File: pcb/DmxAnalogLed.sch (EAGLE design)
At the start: 61 parts, among them IC2 7805TV, J1 RS485, J2 POWER_JACKPTH, J3 RS485, Q1 16MHz 10ppm, U1 ARDUINO_LEONARDO-REV3B_SMARTP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, U2 SN75176ASOIC, X1 USBPTH

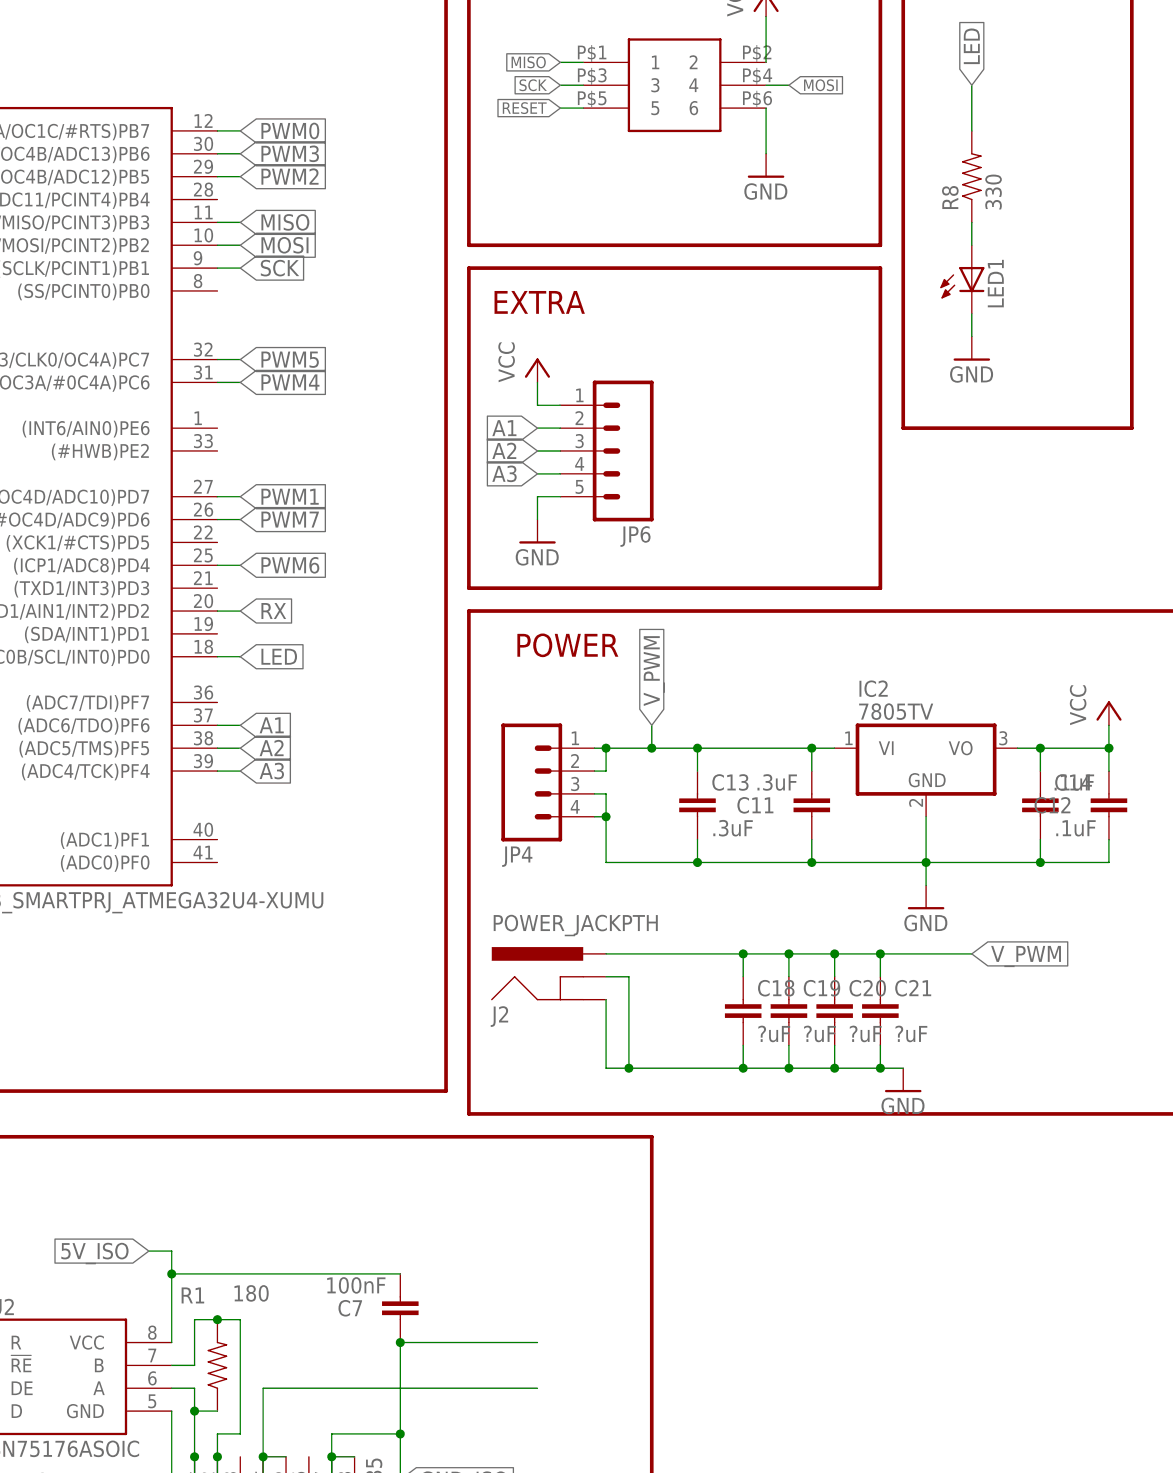
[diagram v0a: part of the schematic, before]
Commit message: Update component values on PCB
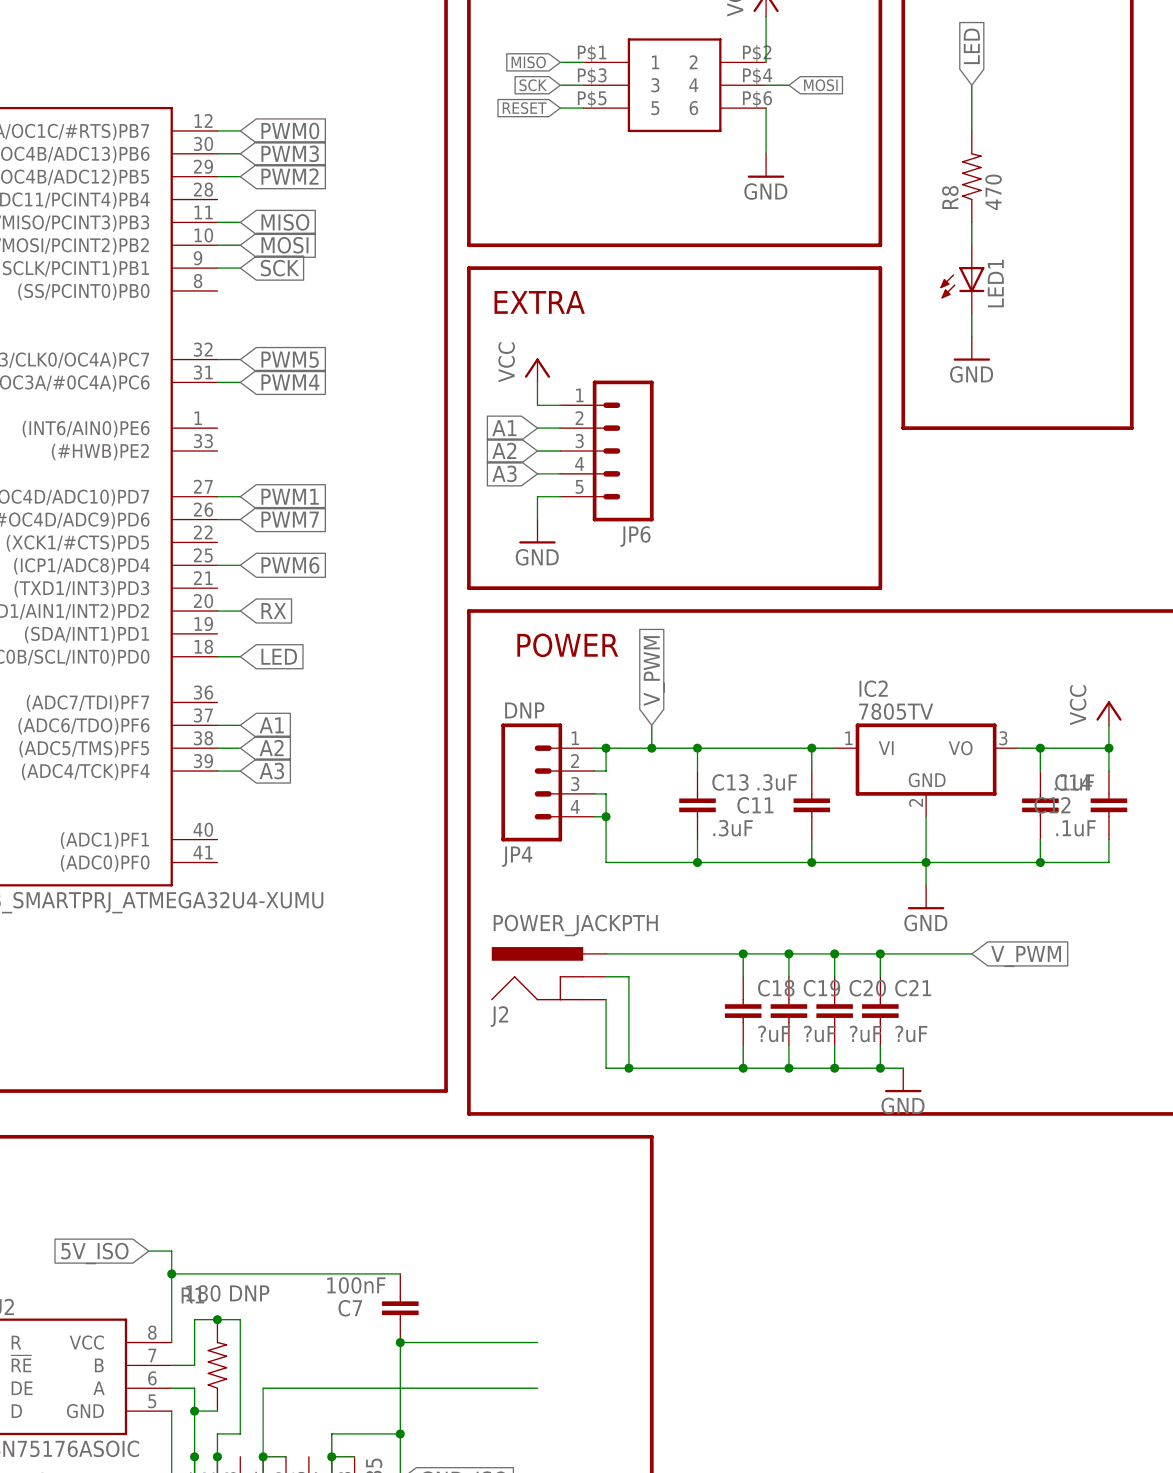
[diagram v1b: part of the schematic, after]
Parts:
- JP4: value (none) -> DNP
- R1: value 180 -> 180 DNP
- R8: value 330 -> 470
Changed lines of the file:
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@@
 <parts>
 <part name="U2" library="reprap" deviceset="SN75176A" device="SOIC"/>
-<part name="R1" library="SparkFun" deviceset="RESISTOR" device="" value="180"/>
+<part name="R1" library="SparkFun" deviceset="RESISTOR" device="" value="180 DNP"/>
 <part name="R2" library="SparkFun" deviceset="RESISTOR" device="" value="10k"/>
-<part name="R8" library="SparkFun" deviceset="RESISTOR" device="" value="330"/>
+<part name="R8" library="SparkFun" deviceset="RESISTOR" device="" value="470"/>
 <part name="GND12" library="supply1" deviceset="GND" device=""/>
 <part name="C7" library="SparkFun" deviceset="CAP" device="0805" value="100nF"/>
@@
 <part name="JP2" library="SparkFun" deviceset="M08" device="3.5MM-8"/>
 <part name="JP3" library="SparkFun" deviceset="M08" device="3.5MM-8"/>
-<part name="JP4" library="SparkFun" deviceset="M04" device="SCREW"/>
+<part name="JP4" library="SparkFun" deviceset="M04" device="SCREW" value="DNP"/>
 <part name="U$10" library="blinkiverse" deviceset="DC_DC_ISOLATED_0505" device=""/>
 <part name="P+8" library="supply1" deviceset="VCC" device=""/>

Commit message: Get RevB ready
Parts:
- removed C18, C19, C20, C21: ?uF, SparkFun:CAP1210
- removed JP4: DNP, SparkFun:M04SCREW
- added C22: .1uF, SparkFun:CAP0805
- added C23, C24, C25, C26: (no value), SparkFun:CAP_POLE
- C3: value 10uF -> .1uF
- C5, C6: value 100nF -> .1uF
- IC2: value 7805TV -> 7805DT; device linear:7805TV -> linear:7805DT
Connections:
- removed net V_PWM: C11.2, C13.1, C18.1, C19.1, C20.1, C21.1, IC2.VI, J2.PWR, JP2.1, JP2.3, JP2.5, JP2.7, JP3.1, JP3.3, JP3.5, JP3.7, JP4.1, JP4.2
- new net V_IN: C11.2, C13.1, C23.+, C24.+, C25.+, C26.+, IC2.VI, J2.PWR, JP2.1, JP2.3, JP2.5, JP2.7, JP3.1, JP3.3, JP3.5, JP3.7
- net GND: now also C22.1, C23.-, C24.-, C25.-, C26.-; no longer C18.2, C19.2, C20.2, C21.2, JP4.3, JP4.4
- net VCC: now also C22.2

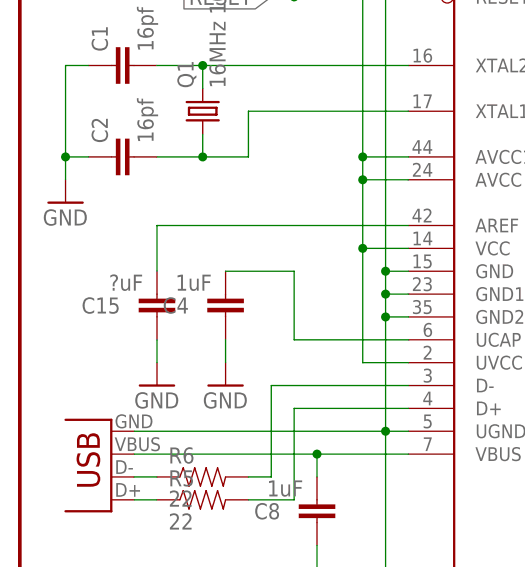
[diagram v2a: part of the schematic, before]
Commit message: RevB candidate; fixes ground plane, isolation, regulator placement, silk.
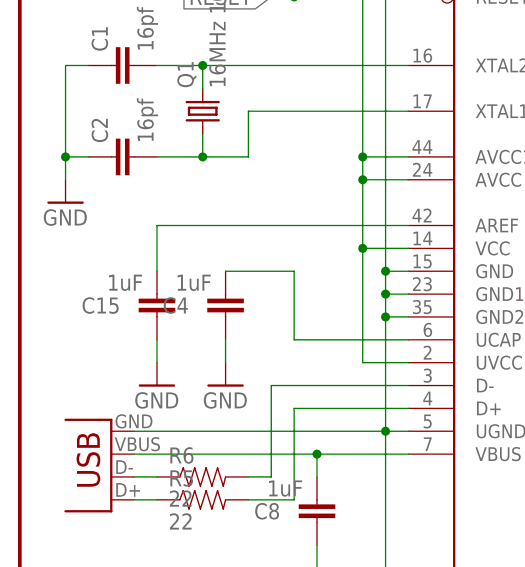
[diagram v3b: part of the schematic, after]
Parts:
- C15: value ?uF -> 1uF
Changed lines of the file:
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@@
 <part name="C13" library="SparkFun" deviceset="CAP" device="1210" value=".3uF"/>
 <part name="C14" library="SparkFun" deviceset="CAP" device="1210" value=".1uF"/>
-<part name="C15" library="SparkFun" deviceset="CAP" device="0805" value="?uF"/>
+<part name="C15" library="SparkFun" deviceset="CAP" device="0805" value="1uF"/>
 <part name="GND3" library="supply1" deviceset="GND" device=""/>
 <part name="C16" library="SparkFun" deviceset="CAP" device="1210" value="4.7uF"/>

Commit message: Make the software faster.
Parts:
- C12, C14, C22, C3, C5, C6: value .1uF -> 100nF
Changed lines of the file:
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@@
 <part name="R5" library="SparkFun" deviceset="RESISTOR" device="" value="22"/>
 <part name="R6" library="SparkFun" deviceset="RESISTOR" device="" value="22"/>
-<part name="C3" library="SparkFun" deviceset="CAP" device="0805" value=".1uF"/>
-<part name="C5" library="SparkFun" deviceset="CAP" device="0805" value=".1uF"/>
-<part name="C6" library="SparkFun" deviceset="CAP" device="0805" value=".1uF"/>
+<part name="C3" library="SparkFun" deviceset="CAP" device="0805" value="100nF"/>
+<part name="C5" library="SparkFun" deviceset="CAP" device="0805" value="100nF"/>
+<part name="C6" library="SparkFun" deviceset="CAP" device="0805" value="100nF"/>
 <part name="GND4" library="supply1" deviceset="GND" device=""/>
 <part name="P+2" library="supply1" deviceset="VCC" device=""/>
@@
 <part name="GND21" library="supply1" deviceset="GND" device=""/>
 <part name="C11" library="SparkFun" deviceset="CAP" device="0805" value=".3uF"/>
-<part name="C12" library="SparkFun" deviceset="CAP" device="0805" value=".1uF"/>
+<part name="C12" library="SparkFun" deviceset="CAP" device="0805" value="100nF"/>
 <part name="JP6" library="SparkFun" deviceset="M05" device="PTH"/>
 <part name="P+3" library="supply1" deviceset="VCC" device=""/>
@@
 <part name="P+4" library="supply1" deviceset="VCC" device=""/>
 <part name="C13" library="SparkFun" deviceset="CAP" device="1210" value=".3uF"/>
-<part name="C14" library="SparkFun" deviceset="CAP" device="1210" value=".1uF"/>
+<part name="C14" library="SparkFun" deviceset="CAP" device="1210" value="100nF"/>
 <part name="C15" library="SparkFun" deviceset="CAP" device="0805" value="1uF"/>
 <part name="GND3" library="supply1" deviceset="GND" device=""/>
@@
 <part name="R16" library="SparkFun" deviceset="RESISTOR" device="" value="10K"/>
 <part name="IC2" library="linear" deviceset="78*" device="DT" technology="05"/>
-<part name="C22" library="SparkFun" deviceset="CAP" device="0805" value=".1uF"/>
+<part name="C22" library="SparkFun" deviceset="CAP" device="0805" value="100nF"/>
 <part name="C23" library="SparkFun" deviceset="CAP_POL" device="E"/>
 <part name="C24" library="SparkFun" deviceset="CAP_POL" device="E"/>

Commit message: Change library name, too
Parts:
- U$1, U$3, U$4, U$5, U$6, U$7, U$8, U$9: device blinkiverse:N_MOSFET -> blinkinlabs:N_MOSFET
- U$10: device blinkiverse:DC_DC_ISOLATED_0505 -> blinkinlabs:DC_DC_ISOLATED_0505
- U1: device blinkiverse:ARDUINO_LEONARDO-REV3B_SMARTPRJ_ATMEGA32U4-XUMU -> blinkinlabs:ARDUINO_LEONARDO-REV3B_SMARTPRJ_ATMEGA32U4-XUMU
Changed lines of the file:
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@@
 <part name="P+5" library="supply1" deviceset="VCC" device=""/>
 <part name="GND10" library="supply1" deviceset="GND" device=""/>
-<part name="U1" library="blinkiverse" deviceset="ARDUINO_LEONARDO-REV3B_SMARTPRJ_ATMEGA32U4-XU" device="MU"/>
+<part name="U1" library="blinkinlabs" deviceset="ARDUINO_LEONARDO-REV3B_SMARTPRJ_ATMEGA32U4-XU" device="MU"/>
 <part name="P+1" library="supply1" deviceset="VCC" device=""/>
 <part name="GND1" library="supply1" deviceset="GND" device=""/>
@@
 <part name="GND6" library="supply1" deviceset="GND" device=""/>
 <part name="J3" library="con-amp" deviceset="520426-4" device="" value="RS485"/>
-<part name="U$1" library="blinkiverse" deviceset="N_MOSFET" device=""/>
+<part name="U$1" library="blinkinlabs" deviceset="N_MOSFET" device=""/>
 <part name="GND7" library="supply1" deviceset="GND" device=""/>
-<part name="U$3" library="blinkiverse" deviceset="N_MOSFET" device=""/>
+<part name="U$3" library="blinkinlabs" deviceset="N_MOSFET" device=""/>
 <part name="GND9" library="supply1" deviceset="GND" device=""/>
-<part name="U$4" library="blinkiverse" deviceset="N_MOSFET" device=""/>
+<part name="U$4" library="blinkinlabs" deviceset="N_MOSFET" device=""/>
 <part name="GND11" library="supply1" deviceset="GND" device=""/>
-<part name="U$5" library="blinkiverse" deviceset="N_MOSFET" device=""/>
+<part name="U$5" library="blinkinlabs" deviceset="N_MOSFET" device=""/>
 <part name="GND13" library="supply1" deviceset="GND" device=""/>
-<part name="U$6" library="blinkiverse" deviceset="N_MOSFET" device=""/>
+<part name="U$6" library="blinkinlabs" deviceset="N_MOSFET" device=""/>
 <part name="GND14" library="supply1" deviceset="GND" device=""/>
-<part name="U$7" library="blinkiverse" deviceset="N_MOSFET" device=""/>
+<part name="U$7" library="blinkinlabs" deviceset="N_MOSFET" device=""/>
 <part name="GND15" library="supply1" deviceset="GND" device=""/>
-<part name="U$8" library="blinkiverse" deviceset="N_MOSFET" device=""/>
+<part name="U$8" library="blinkinlabs" deviceset="N_MOSFET" device=""/>
 <part name="GND16" library="supply1" deviceset="GND" device=""/>
-<part name="U$9" library="blinkiverse" deviceset="N_MOSFET" device=""/>
+<part name="U$9" library="blinkinlabs" deviceset="N_MOSFET" device=""/>
 <part name="GND17" library="supply1" deviceset="GND" device=""/>
 <part name="JP2" library="SparkFun" deviceset="M08" device="3.5MM-8"/>
 <part name="JP3" library="SparkFun" deviceset="M08" device="3.5MM-8"/>
-<part name="U$10" library="blinkiverse" deviceset="DC_DC_ISOLATED_0505" device=""/>
+<part name="U$10" library="blinkinlabs" deviceset="DC_DC_ISOLATED_0505" device=""/>
 <part name="P+8" library="supply1" deviceset="VCC" device=""/>
 <part name="GND20" library="SparkFun" deviceset="GND" device=""/>
